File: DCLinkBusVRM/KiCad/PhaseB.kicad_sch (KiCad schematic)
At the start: 34 parts, among them IC9 LM358DR, Q2 IMBG65R015M2H, Q5 IMBG65R015M2H, U1 ACS758xCB-200U-PFF

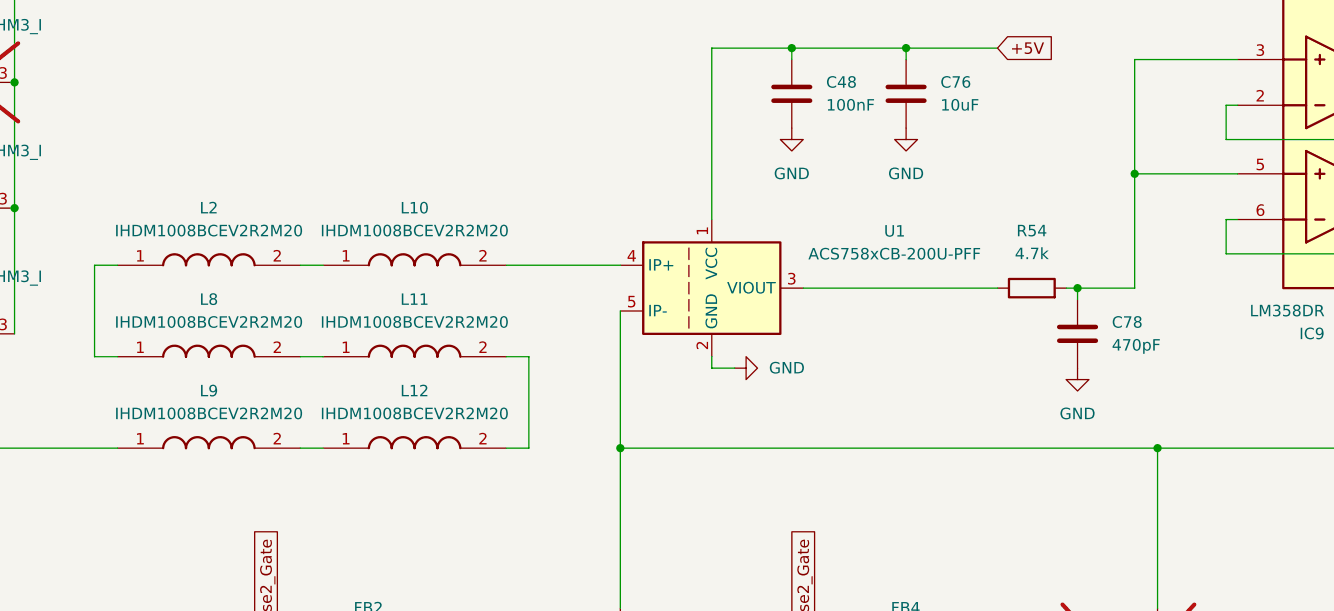
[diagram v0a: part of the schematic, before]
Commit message: Update boost converter, add dynamic brake grid, etc
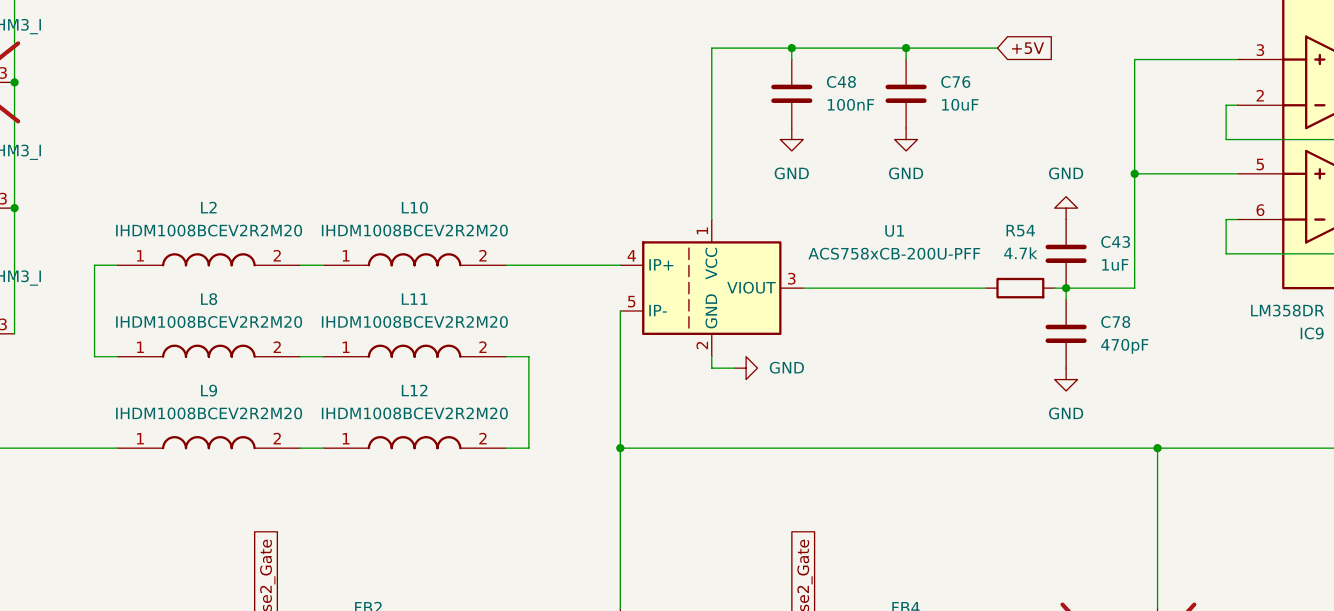
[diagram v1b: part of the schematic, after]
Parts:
- added C43: 1uF, Capacitor_SMD:C_1210_3225Metric_Pad1.33x2.70mm_HandSolder, symbol Device:C
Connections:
- net GND: now also C43.1
- net at C78.1, IC9.3 (IN1+), IC9.5 (IN2+)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: now also C43.2
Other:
- moved on the sheet: C78, R54
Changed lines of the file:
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@@
 (kicad_sch
-	(version 20231120)
+	(version 20250114)
 	(generator "eeschema")
-	(generator_version "8.0")
+	(generator_version "9.0")
 	(paper "A4")
 	(title_block
@@
 	)
 	(junction
-		(at 171.45 77.47)
+		(at 255.27 96.52)
 		(diameter 0)
 		(color 0 0 0 0)
 	)
 	(junction
-		(at 255.27 96.52)
+		(at 43.18 71.12)
 		(diameter 0)
 		(color 0 0 0 0)
 	)
 	(junction
-		(at 43.18 71.12)
+		(at 170.18 77.47)
 		(diameter 0)
 		(color 0 0 0 0)
@@
 	(wire
 		(pts
-			(xy 140.97 77.47) (xy 162.56 77.47)
+			(xy 140.97 77.47) (xy 161.29 77.47)
 		)
 		(stroke
@@
 	(wire
 		(pts
+			(xy 168.91 77.47) (xy 170.18 77.47)
+		)
+		(stroke
+			(width 0)
+			(type default)
+		)
+	)
+	(wire
+		(pts
 			(xy 148.59 120.65) (xy 140.97 120.65)
 		)
@@
 	(wire
 		(pts
-			(xy 171.45 77.47) (xy 177.8 77.47)
-		)
-		(stroke
-			(width 0)
-			(type default)
-		)
-	)
-	(wire
-		(pts
 			(xy 62.23 74.93) (xy 64.77 74.93)
 		)
@@
 	(wire
 		(pts
-			(xy 170.18 77.47) (xy 171.45 77.47)
+			(xy 170.18 77.47) (xy 177.8 77.47)
 		)
 		(stroke
@@
 	(wire
 		(pts
-			(xy 171.45 77.47) (xy 171.45 78.74)
+			(xy 170.18 77.47) (xy 170.18 78.74)
 		)
 		(stroke
@@
 	(symbol
 		(lib_id "Device:C")
-		(at 171.45 82.55 0)
+		(at 170.18 82.55 0)
 		(unit 1)
 		(exclude_from_sim no)
@@
 		(fields_autoplaced yes)
 		(property "Reference" "C78"
-			(at 175.26 81.2799 0)
+			(at 173.99 81.2799 0)
 			(effects
 				(font
@@
 		)
 		(property "Value" "470pF"
-			(at 175.26 83.8199 0)
+			(at 173.99 83.8199 0)
 			(effects
 				(font
@@
 		)
 		(property "Footprint" "Capacitor_SMD:C_1210_3225Metric_Pad1.33x2.70mm_HandSolder"
-			(at 172.4152 86.36 0)
+			(at 171.1452 86.36 0)
 			(effects
 				(font
@@
 		)
 		(property "Datasheet" "~"
-			(at 171.45 82.55 0)
+			(at 170.18 82.55 0)
 			(effects
 				(font
@@
 		)
 		(property "Description" "Unpolarized capacitor"
-			(at 171.45 82.55 0)
+			(at 170.18 82.55 0)
 			(effects
 				(font
@@
 	(symbol
 		(lib_id "power:GND")
-		(at 171.45 86.36 0)
+		(at 170.18 86.36 0)
 		(unit 1)
 		(exclude_from_sim no)
@@
 		(fields_autoplaced yes)
 		(property "Reference" "#PWR0104"
-			(at 171.45 92.71 0)
+			(at 170.18 92.71 0)
 			(effects
 				(font
@@
 		)
 		(property "Value" "GND"
-			(at 171.45 91.44 0)
+			(at 170.18 91.44 0)
 			(effects
 				(font
@@
 		)
 		(property "Footprint" ""
-			(at 171.45 86.36 0)
+			(at 170.18 86.36 0)
 			(effects
 				(font
@@
 		)
 		(property "Datasheet" ""
-			(at 171.45 86.36 0)
+			(at 170.18 86.36 0)
 			(effects
 				(font
@@
 		)
 		(property "Description" "Power symbol creates a global label with name \"GND\" , ground"
-			(at 171.45 86.36 0)
+			(at 170.18 86.36 0)
 			(effects
 				(font
@@
 	(symbol
 		(lib_id "Device:R")
-		(at 166.37 77.47 90)
+		(at 165.1 77.47 90)
 		(unit 1)
 		(exclude_from_sim no)
@@
 		(fields_autoplaced yes)
 		(property "Reference" "R54"
-			(at 166.37 71.12 90)
+			(at 165.1 71.12 90)
 			(effects
 				(font
@@
 		)
 		(property "Value" "4.7k"
-			(at 166.37 73.66 90)
+			(at 165.1 73.66 90)
 			(effects
 				(font
@@
 		)
 		(property "Footprint" "Resistor_SMD:R_1210_3225Metric_Pad1.30x2.65mm_HandSolder"
-			(at 166.37 79.248 90)
+			(at 165.1 79.248 90)
 			(effects
 				(font
@@
 		)
 		(property "Datasheet" "~"
-			(at 166.37 77.47 0)
+			(at 165.1 77.47 0)
 			(effects
 				(font
@@
 		)
 		(property "Description" "Resistor"
-			(at 166.37 77.47 0)
+			(at 165.1 77.47 0)
 			(effects
 				(font
@@
 	)
 	(symbol
+		(lib_id "power:GND")
+		(at 170.18 69.85 180)
+		(unit 1)
+		(exclude_from_sim no)
+		(in_bom yes)
+		(on_board yes)
+		(dnp no)
+		(fields_autoplaced yes)
+		(property "Reference" "#PWR0110"
+			(at 170.18 63.5 0)
+			(effects
+				(font
+					(size 1.27 1.27)
+				)
+				(hide yes)
+			)
+		)
+		(property "Value" "GND"
+			(at 170.18 64.77 0)
+			(effects
+				(font
+					(size 1.27 1.27)
+				)
+			)
+		)
+		(property "Footprint" ""
+			(at 170.18 69.85 0)
+			(effects
+				(font
+					(size 1.27 1.27)
+				)
+				(hide yes)
+			)
+		)
+		(property "Datasheet" ""
+			(at 170.18 69.85 0)
+			(effects
+				(font
+					(size 1.27 1.27)
+				)
+				(hide yes)
+			)
+		)
+		(property "Description" "Power symbol creates a global label with name \"GND\" , ground"
+			(at 170.18 69.85 0)
+			(effects
+				(font
+					(size 1.27 1.27)
+				)
+				(hide yes)
+			)
+		)
+		(pin "1"
+		)
+		(instances
+			(project "InverterBoostConverter_v2"
+				(path "/2b0bf6ef-6fb8-4b0f-8d72-c07d92ef1505/6b8c86c7-5ef6-49d8-97f5-34ef0211a71f"
+					(reference "#PWR0110")
+					(unit 1)
+				)
+			)
+		)
+	)
+	(symbol
 		(lib_id "Device:D_Dual_CommonCathode_AAK_Parallel")
 		(at 250.19 68.58 0)
@@
 					(unit 1)
 				)
+			)
+		)
+	)
+	(symbol
+		(lib_id "Device:C")
+		(at 170.18 73.66 0)
+		(unit 1)
+		(exclude_from_sim no)
+		(in_bom yes)
+		(on_board yes)
+		(dnp no)
+		(fields_autoplaced yes)
+		(property "Reference" "C43"
+			(at 173.99 72.3899 0)
+			(effects
+				(font
+					(size 1.27 1.27)
+				)
+				(justify left)
+			)
+		)
+		(property "Value" "1uF"
+			(at 173.99 74.9299 0)
+			(effects
+				(font
+					(size 1.27 1.27)
+				)
+				(justify left)
+			)
+		)
+		(property "Footprint" "Capacitor_SMD:C_1210_3225Metric_Pad1.33x2.70mm_HandSolder"
+			(at 171.1452 77.47 0)
+			(effects
+				(font
+					(size 1.27 1.27)
+				)
+				(hide yes)
+			)
+		)
+		(property "Datasheet" "~"
+			(at 170.18 73.66 0)
+			(effects
+				(font
+					(size 1.27 1.27)
+				)
+				(hide yes)
+			)
+		)
+		(property "Description" "Unpolarized capacitor"
+			(at 170.18 73.66 0)
+			(effects
+				(font
+					(size 1.27 1.27)
+				)
+				(hide yes)
+			)
+		)
+		(pin "1"
+		)
+		(pin "2"
+		)
+		(instances
+			(project "InverterBoostConverter_v2"
+				(path "/2b0bf6ef-6fb8-4b0f-8d72-c07d92ef1505/6b8c86c7-5ef6-49d8-97f5-34ef0211a71f"
+					(reference "C43")
+					(unit 1)
+				)

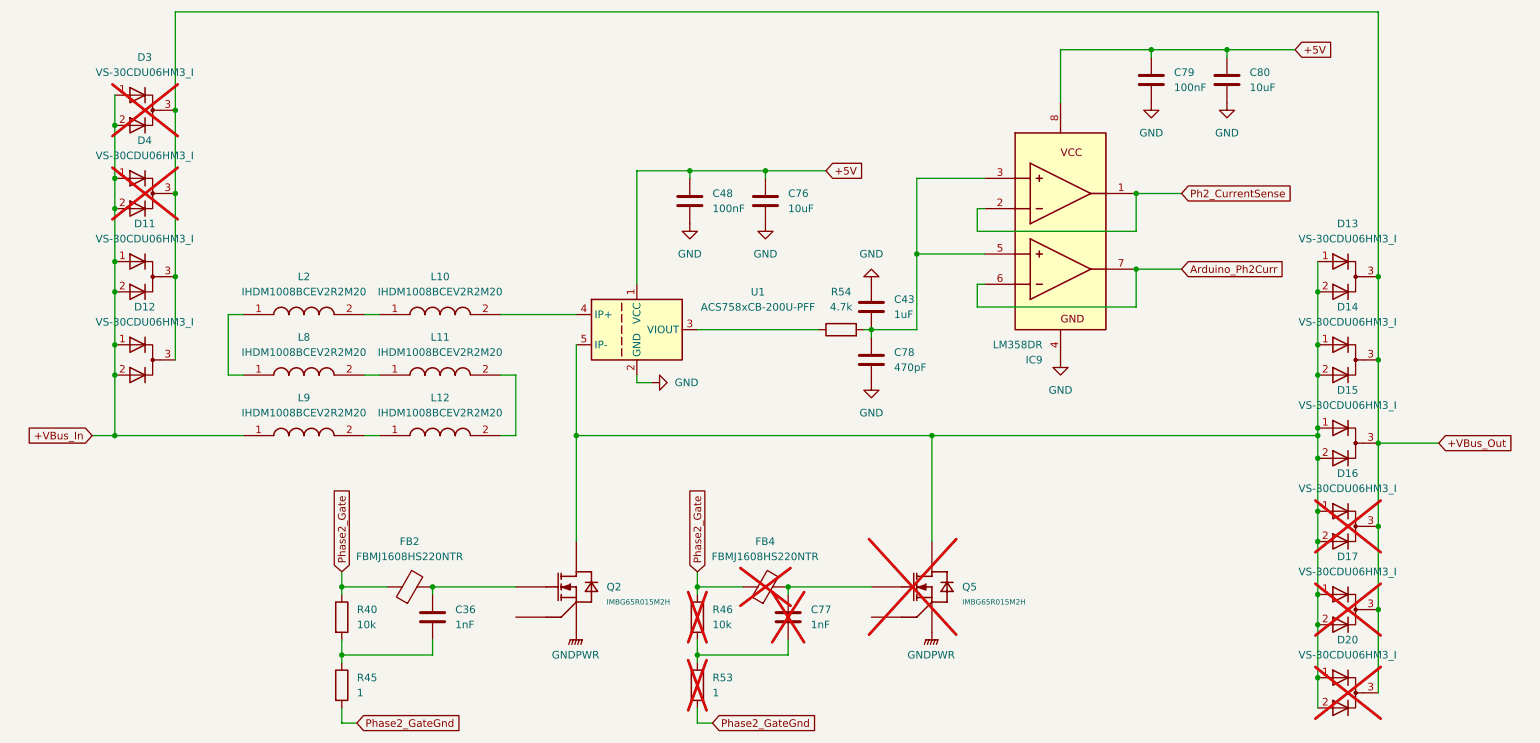
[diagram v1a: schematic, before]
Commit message: Update Canbus protocol for vrm
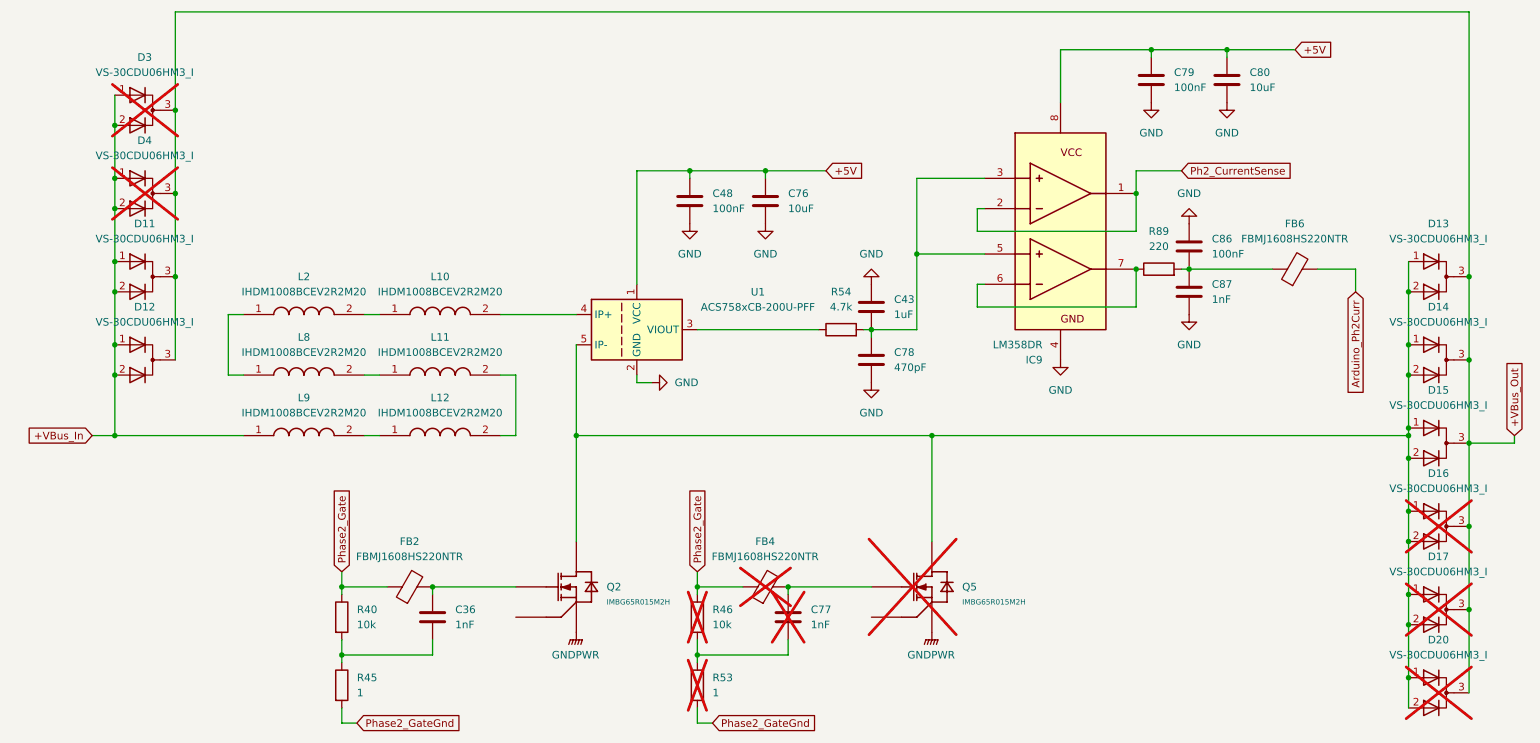
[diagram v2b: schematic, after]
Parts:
- added C86: 100nF, Capacitor_SMD:C_1210_3225Metric_Pad1.33x2.70mm_HandSolder, symbol Device:C
- added C87: 1nF, Capacitor_SMD:C_1210_3225Metric_Pad1.33x2.70mm_HandSolder, symbol Device:C
- added FB6: FBMJ1608HS220NTR, InverterCom:BEADC1608X100N, symbol Device:FerriteBead
- added R89: 220, Resistor_SMD:R_1210_3225Metric_Pad1.30x2.65mm_HandSolder, symbol Device:R
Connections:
- net Arduino_Ph2Curr: now also FB6.2; no longer IC9.6 (IN2-), IC9.7 (OUT2)
- net GND: now also C86.1, C87.1
- new net: C86.2, C87.2, FB6.1, R89.2
- new net: IC9.6 (IN2-), IC9.7 (OUT2), R89.1
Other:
- moved on the sheet: D13, D14, D15, D16, D17, D20
